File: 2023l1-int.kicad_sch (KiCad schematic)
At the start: 157 parts, among them J1 52610-1433, J8 XT60, Q1 STP75NF75, SW4 SW_SPDT, U1 LM2587

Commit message: idl kicad
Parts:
- removed C1: 220u, footprints:EIA-7343-D, symbol Device:C_Polarized
- removed C2: 1u, footprints:cap0603, symbol Device:C
- removed D1: SS510, footprints:DIOM5025X220N, symbol SS510-HF:SS510-HF
- removed L1: 56µH, footprints:L_Sunlord_SWPA8040S, symbol Device:L
- removed R1: 2K94, footprints:res0603, symbol Device:R
- removed R2: 57K, footprints:res0603, symbol Device:R
- removed R3: 1K5, footprints:res0603, symbol Device:R
- removed TRIMPOT1: 10K, footprints:3362W1201LF, symbol Device:R_Potentiometer
- removed U1: LM2587, footprints:TO170P1435X465-6N, symbol LM2587S-ADJ_NOPB:LM2587S-ADJ_NOPB

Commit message: kill me
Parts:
- added Boost1: ~, footprints:Boost, symbol Boost:Boost
- SW?: footprint footprints:SS12D00G3 -> Connector_PinHeader_2.54mm:PinHeader_1x03_P2.54mm_Vertical
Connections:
- net +12V: now also Boost1.1 (VIN)
- net +48V: now also Boost1.2 (VOUT)
- net GND: now also Boost1.3 (GND), Boost1.4 (GND)
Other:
- moved on the sheet: C?

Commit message: I HATE DOING L1
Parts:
- removed SW4: SW_SPDT, footprints:SS12D00G3, symbol Switch:SW_SPDT
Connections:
- net +3V3: now also J?.1 (Pin_1)
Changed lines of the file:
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@@
     (stroke (width 0) (type default))
   )
-  (wire (pts (xy 295.91 180.34) (xy 288.29 180.34))
-    (stroke (width 0) (type default))
-  )
   (wire (pts (xy 49.53 35.56) (xy 58.42 35.56))
     (stroke (width 0) (type default))
@@
     (stroke (width 0) (type default))
   )
-  (wire (pts (xy 273.05 177.8) (xy 278.13 177.8))
+  (wire (pts (xy 288.29 180.34) (xy 295.91 180.34))
     (stroke (width 0) (type default))
   )
@@
     )
   )
-  (symbol (lib_id "power:+3V3") (at 273.05 177.8 90) (mirror x) (unit 1)
+  (symbol (lib_id "power:+3V3") (at 288.29 180.34 90) (mirror x) (unit 1)
     (in_bom yes) (on_board yes) (dnp no) (fields_autoplaced)
-    (property "Reference" "#PWR?" (at 276.86 177.8 0)
+    (property "Reference" "#PWR?" (at 292.1 180.34 0)
       (effects (font (size 1.27 1.27)) hide)
     )
-    (property "Value" "+3V3" (at 269.24 177.8 90)
+    (property "Value" "+3V3" (at 284.48 180.34 90)
       (effects (font (size 1.27 1.27)) (justify left))
     )
-    (property "Footprint" "" (at 273.05 177.8 0)
+    (property "Footprint" "" (at 288.29 180.34 0)
       (effects (font (size 1.27 1.27)) hide)
     )
-    (property "Datasheet" "" (at 273.05 177.8 0)
+    (property "Datasheet" "" (at 288.29 180.34 0)
       (effects (font (size 1.27 1.27)) hide)
     )
@@
         )
       )
-    )
-  )
-  (symbol (lib_id "Switch:SW_SPDT") (at 283.21 180.34 0) (mirror y) (unit 1)
-    (in_bom yes) (on_board yes) (dnp no) (fields_autoplaced)
-    (property "Reference" "SW4" (at 283.21 173.99 0)
-      (effects (font (size 1.27 1.27)))
-    )
-    (property "Value" "SW_SPDT" (at 283.21 176.53 0)
-      (effects (font (size 1.27 1.27)))
-    )
-    (property "Footprint" "footprints:SS12D00G3" (at 283.21 180.34 0)
-      (effects (font (size 1.27 1.27)) hide)
-    )
-    (property "Datasheet" "~" (at 283.21 180.34 0)
-      (effects (font (size 1.27 1.27)) hide)
-    )
-    (pin "1")
-    (pin "2")
-    (pin "3")
-    (instances
-      (project "2023l1-int"
-        (path "/dd82140d-c14c-4d8d-8674-edeceaca486e"
-          (reference "SW4") (unit 1)
-        )
-      )

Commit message: left with boost
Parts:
- removed C? (x2): 10u, footprints:cap0603, symbol Device:C
- removed C? (x2): 220u, footprints:EIA-7343-D, symbol Device:C_Polarized
- removed C? (x2): 10n, footprints:cap0603, symbol Device:C
- removed D? (x2): SS54, footprints:DIOM5025X220N, symbol Diode:B340
- removed L? (x2): 15u, footprints:L_Sunlord_SWPA8040S, symbol Device:L_Iron
- removed R?: 5K9, footprints:res0603, symbol Device:R
- removed R? (x2): 10K, footprints:res0603, symbol Device:R
- removed R?: 3K24, footprints:res0603, symbol Device:R
- removed U? (x2): TPS5430DDA, Package_SO:TI_SO-PowerPAD-8_ThermalVias, symbol Regulator_Switching:TPS5430DDA
- added U1, U3: ~, footprints:buck, symbol buck:buck
- J1: footprint footprints:0526101433 -> footprints:526101433
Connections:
- net +12V: now also U1.VIN, U3.VIN
- net +3V3: now also U1.VOUT
- net +5V: now also U3.VOUT
- net GND: now also U1.GND, U3.GND
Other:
- note removed: "12V - 3V3"
- note removed: "12V - 5V"

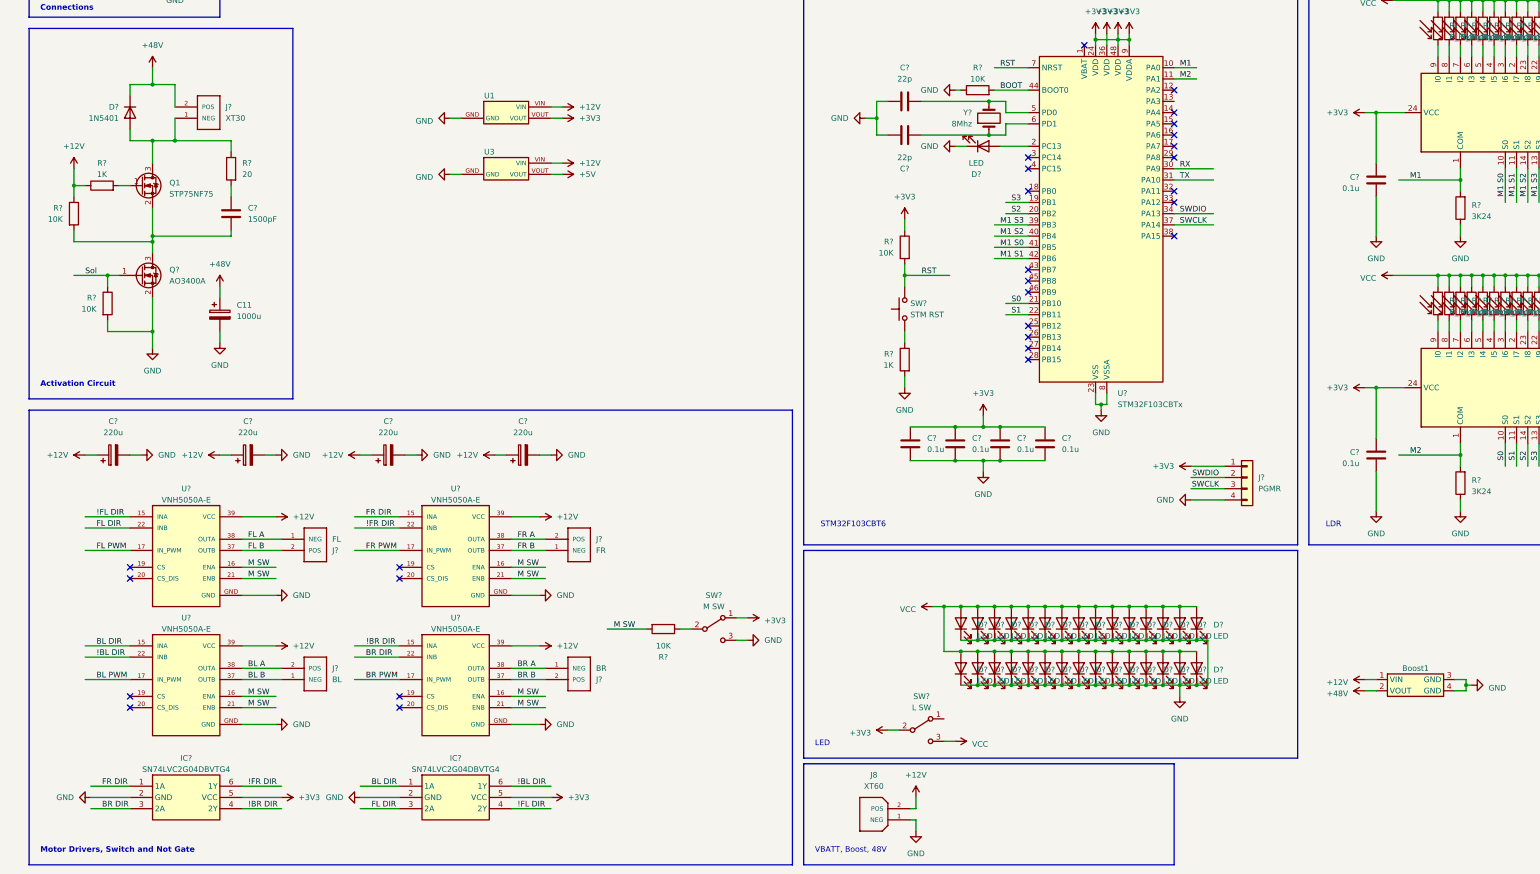
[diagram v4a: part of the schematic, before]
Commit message: done component placement
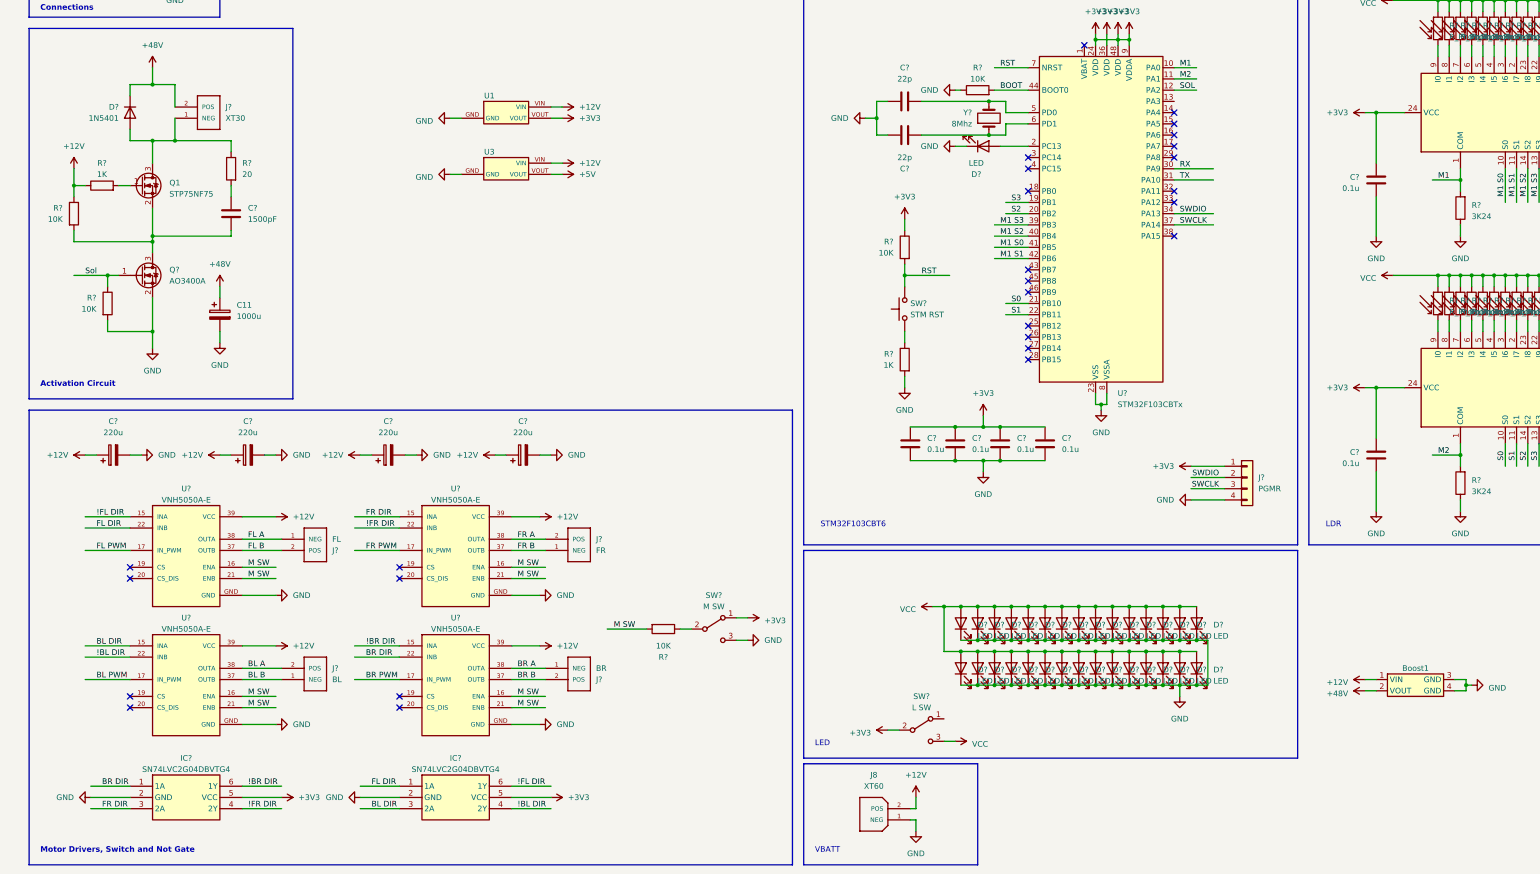
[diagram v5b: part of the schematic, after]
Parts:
- Boost1: footprint footprints:Boost -> footprints:boost
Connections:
- net !BL DIR: now also IC?.4 (2Y); no longer IC?.6 (1Y)
- net !BR DIR: now also IC?.6 (1Y); no longer IC?.4 (2Y)
- net !FL DIR: now also IC?.6 (1Y); no longer IC?.4 (2Y)
- net !FR DIR: now also IC?.4 (2Y); no longer IC?.6 (1Y)
- net BL DIR: now also IC?.3 (2A); no longer IC?.1 (1A)
- net BR DIR: now also IC?.1 (1A); no longer IC?.3 (2A)
- net FL DIR: now also IC?.1 (1A); no longer IC?.3 (2A)
- net FR DIR: now also IC?.3 (2A); no longer IC?.1 (1A)
- net SOL: now reaches U?.12 (PA2)
- no-connect marks 30 -> 29
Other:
- note added: "VBATT"
- note removed: "VBATT, Boost, 48V"

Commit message: mux wiring done
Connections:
- net Sol: now also U?.29 (PA8)
- net SOL: no longer names the net of U?.12 (PA2)
- no-connect marks 29 -> 30
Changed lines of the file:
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@@
   (no_connect (at 284.48 102.87))
   (no_connect (at 284.48 118.11))
-  (no_connect (at 284.48 110.49))
   (no_connect (at 284.48 128.27))
   (no_connect (at 284.48 105.41))
@@
   (no_connect (at 251.46 140.97))
   (no_connect (at 109.22 232.41))
+  (no_connect (at 284.48 97.79))
   (no_connect (at 48.26 205.74))
   (no_connect (at 251.46 138.43))
@@
   (no_connect (at 284.48 120.65))
   (no_connect (at 109.22 234.95))
+  (no_connect (at 284.48 95.25))
   (no_connect (at 251.46 151.13))
   (bus_entry (at 17.78 11.43) (size 2.54 2.54)
@@
     (stroke (width 0) (type default))
   )
-  (wire (pts (xy 284.48 113.03) (xy 293.37 113.03))
-    (stroke (width 0) (type default))
-  )
   (wire (pts (xy 361.95 74.93) (xy 361.95 77.47))
     (stroke (width 0) (type default))
@@
     (stroke (width 0) (type default))
   )
-  (wire (pts (xy 284.48 95.25) (xy 289.56 95.25))
-    (stroke (width 0) (type default))
-  )
   (wire (pts (xy 49.53 58.42) (xy 58.42 58.42))
     (stroke (width 0) (type default))
@@
     (stroke (width 0) (type default))
   )
+  (wire (pts (xy 284.48 110.49) (xy 289.56 110.49))
+    (stroke (width 0) (type default))
+  )
   (wire (pts (xy 49.53 43.18) (xy 57.15 43.18))
     (stroke (width 0) (type default))
@@
     (stroke (width 0) (type default))
   )
+  (wire (pts (xy 284.48 115.57) (xy 289.56 115.57))
+    (stroke (width 0) (type default))
+  )
   (wire (pts (xy 73.66 228.6) (xy 82.55 228.6))
     (stroke (width 0) (type default))
@@
     (stroke (width 0) (type default))
   )
+  (wire (pts (xy 284.48 113.03) (xy 289.56 113.03))
+    (stroke (width 0) (type default))
+  )
   (wire (pts (xy 356.87 74.93) (xy 356.87 77.47))
     (stroke (width 0) (type default))
@@
   )
   (wire (pts (xy 351.79 137.16) (xy 349.25 137.16))
-    (stroke (width 0) (type default))
-  )
-  (wire (pts (xy 284.48 115.57) (xy 293.37 115.57))
     (stroke (width 0) (type default))
   )
@@
     (effects (font (size 1.27 1.27)) (justify left bottom))
   )
-  (label "SOL" (at 285.75 95.25 0) (fields_autoplaced)
-    (effects (font (size 1.27 1.27)) (justify left bottom))
-  )
   (label "M SW" (at 74.93 203.2 0) (fields_autoplaced)
     (effects (font (size 1.27 1.27)) (justify left bottom))
@@
     (effects (font (size 1.27 1.27)) (justify left bottom))
   )
+  (label "Sol" (at 285.75 110.49 0) (fields_autoplaced)
+    (effects (font (size 1.27 1.27)) (justify left bottom))
+  )

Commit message: time to do it again
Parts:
- removed SW?: L SW, Connector_PinHeader_2.54mm:PinHeader_1x03_P2.54mm_Vertical, symbol Switch:SW_SPDT
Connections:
- net VCC is gone; now on net +3V3: D?.2 (A), D?.2 (A), D?.2 (A), D?.2 (A), D?.2 (A), D?.2 (A), D?.2 (A), D?.2 (A), D?.2 (A), D?.2 (A), D?.2 (A), D?.2 (A), D?.2 (A), D?.2 (A), D?.2 (A), D?.2 (A), D?.2 (A), D?.2 (A), D?.2 (A), D?.2 (A), D?.2 (A), D?.2 (A), D?.2 (A), D?.2 (A), D?.2 (A), D?.2 (A), D?.2 (A), D?.2 (A), D?.2 (A), D?.2 (A), R?.1, R?.1, R?.1, R?.1, R?.1, R?.1, R?.1, R?.1, R?.1, R?.1, R?.1, R?.1, R?.1, R?.1, R?.1, R?.1, R?.1, R?.1, R?.1, R?.1, R?.1, R?.1, R?.1, R?.1, R?.1, R?.1, R?.1, R?.1, R?.1, R?.1
- net M1: now also U?.16 (PA6); no longer U?.10 (PA0)
- net M1 S0: now also U?.42 (PB6); no longer U?.41 (PB5)
- net M1 S1: now also U?.43 (PB7); no longer U?.42 (PB6)
- net M1 S2: now also U?.41 (PB5); no longer U?.40 (PB4)
- net M1 S3: now also U?.40 (PB4); no longer U?.39 (PB3)
- net M2: now also U?.19 (PB1); no longer U?.11 (PA1)
- net S0: now also U?.20 (PB2); no longer U?.21 (PB10)
- net S1: now also U?.21 (PB10); no longer U?.22 (PB11)
- net S2: now also U?.18 (PB0); no longer U?.20 (PB2)
- net S3: now also U?.17 (PA7); no longer U?.19 (PB1)

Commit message: transitioning
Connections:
- net !BR DIR: now also IC?.6 (1Y); no longer IC?.6 (1Y)
- net !FL DIR: now also IC?.4 (2Y); no longer IC?.6 (1Y)
- net !FR DIR: now also IC?.6 (1Y); no longer IC?.4 (2Y)
- net BR DIR: now also IC?.1 (1A); no longer IC?.1 (1A)
- net FL DIR: now also IC?.3 (2A); no longer IC?.1 (1A)
- net FR DIR: now also IC?.1 (1A); no longer IC?.3 (2A)
